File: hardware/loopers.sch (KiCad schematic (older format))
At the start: 2 parts

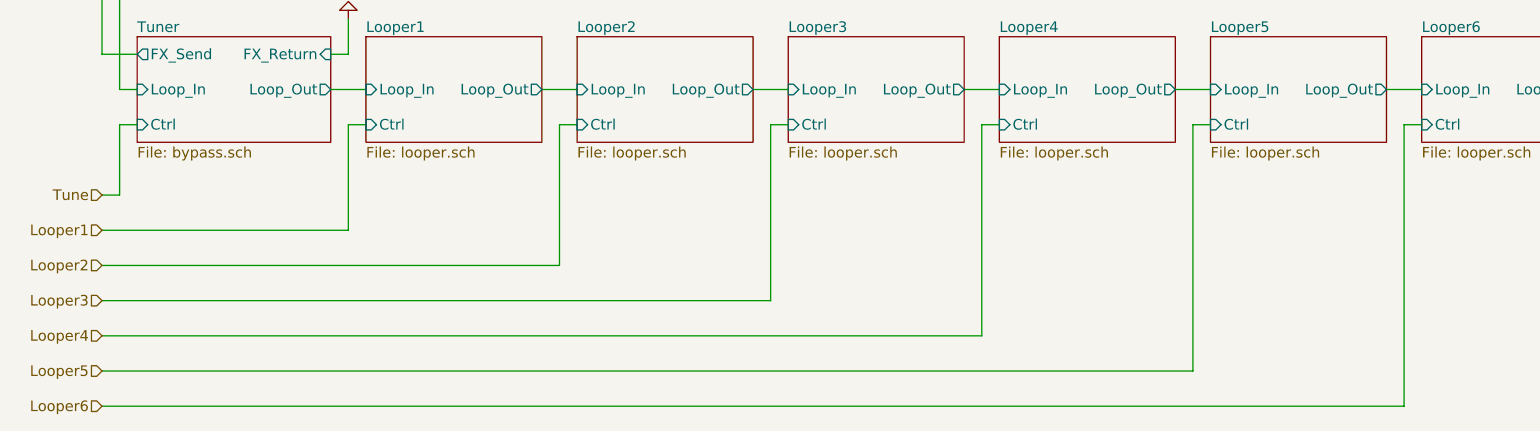
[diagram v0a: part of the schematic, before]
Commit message: Tidy up loopers schematic
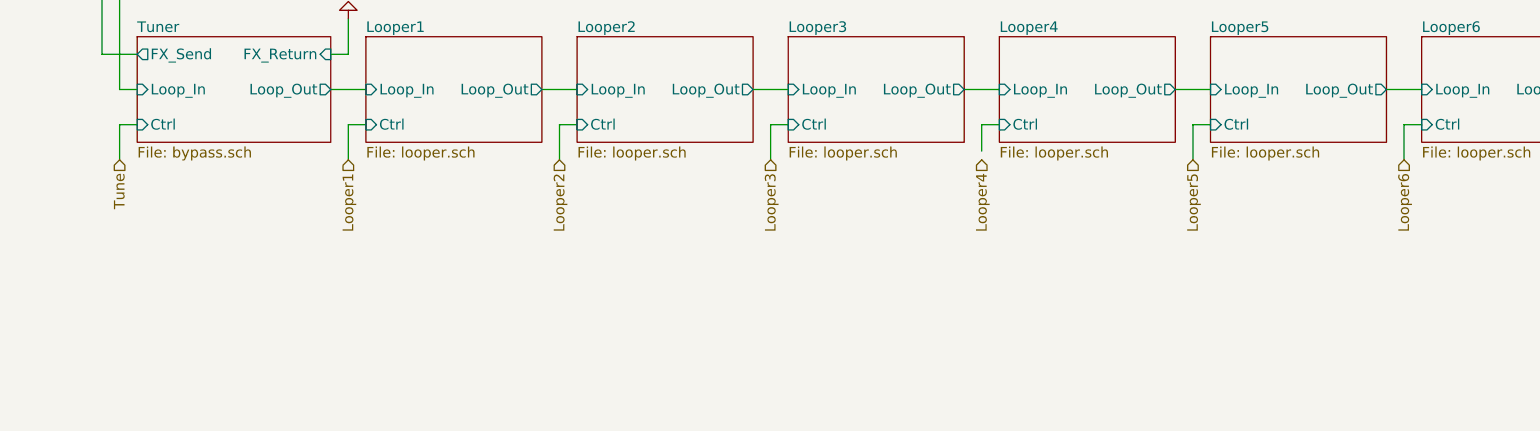
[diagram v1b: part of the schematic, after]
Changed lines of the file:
@@
 Wire Wire Line
 	2500 3200 2500 3000
-Text HLabel 1100 4000 0    60   Input ~ 0
+Text HLabel 1200 3800 3    60   Input ~ 0
 Tune
-Text HLabel 1100 4200 0    60   Input ~ 0
+Text HLabel 2500 3800 3    60   Input ~ 0
 Looper1
-Text HLabel 1100 4400 0    60   Input ~ 0
+Text HLabel 3700 3800 3    60   Input ~ 0
 Looper2
-Text HLabel 1100 4600 0    60   Input ~ 0
+Text HLabel 4900 3800 3    60   Input ~ 0
 Looper3
-Text HLabel 1100 4800 0    60   Input ~ 0
+Text HLabel 6100 3800 3    60   Input ~ 0
 Looper4
-Text HLabel 1100 5000 0    60   Input ~ 0
+Text HLabel 7300 3800 3    60   Input ~ 0
 Looper5
-Text HLabel 1100 5200 0    60   Input ~ 0
+Text HLabel 8500 3800 3    60   Input ~ 0
 Looper6
-Wire Wire Line
-	1200 4000 1200 3600
 Wire Wire Line
 	1200 3600 1300 3600
 Wire Wire Line
-	1100 4000 1200 4000
-Wire Wire Line
-	1100 4200 2500 4200
-Wire Wire Line
-	2500 4200 2500 3600
-Wire Wire Line
 	2500 3600 2600 3600
-Wire Wire Line
-	1100 4400 3700 4400
-Wire Wire Line
-	3700 4400 3700 3600
 Wire Wire Line
 	3700 3600 3800 3600
 Wire Wire Line
-	1100 4600 4900 4600
-Wire Wire Line
-	4900 4600 4900 3600
-Wire Wire Line
 	4900 3600 5000 3600
-Wire Wire Line
-	1100 4800 6100 4800
-Wire Wire Line
-	6100 4800 6100 3600
 Wire Wire Line
 	6100 3600 6200 3600
 Wire Wire Line
-	1100 5000 7300 5000
-Wire Wire Line
-	7300 5000 7300 3600
-Wire Wire Line
 	7300 3600 7400 3600
 Wire Wire Line
-	1100 5200 8500 5200
+	8500 3600 8600 3600
 Wire Wire Line
-	8500 5200 8500 3600
+	8500 3800 8500 3600
 Wire Wire Line
-	8500 3600 8600 3600
+	1200 3800 1200 3600
+Wire Wire Line
+	2500 3600 2500 3800
+Wire Wire Line
+	3700 3800 3700 3600
+Wire Wire Line
+	4900 3800 4900 3600
+Wire Wire Line
+	6100 3750 6100 3600
+Wire Wire Line
+	7300 3800 7300 3600
 $EndSCHEMATC

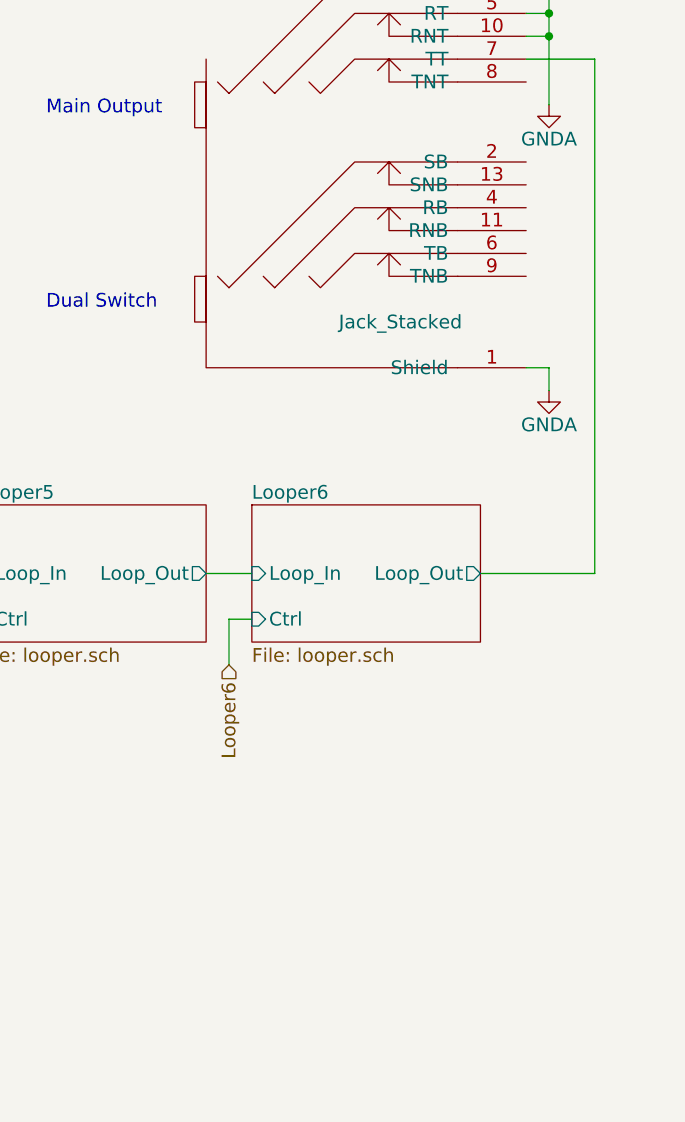
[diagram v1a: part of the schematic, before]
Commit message: Stub and integrate aux switch
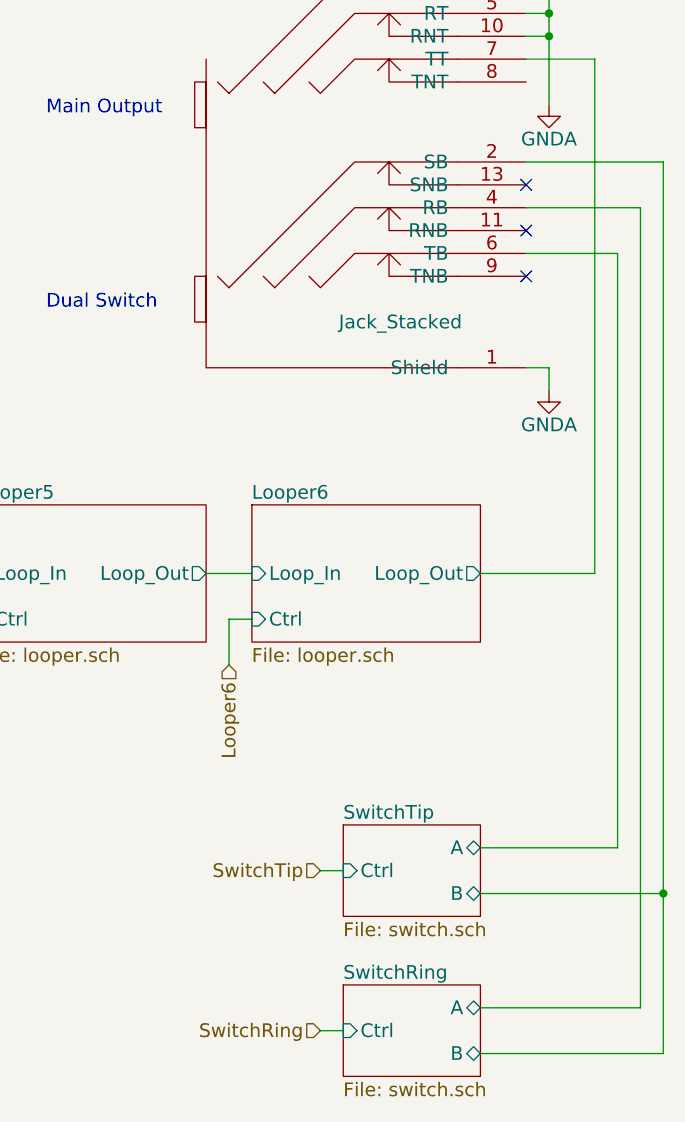
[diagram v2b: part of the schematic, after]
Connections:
- net SwitchRing/B: now reaches CON?.2 (SB)
- net SwitchRing/A: now reaches CON?.4 (RB)
- net SwitchTip/A: now reaches CON?.6 (TB)
- no-connect marks 0 -> 3
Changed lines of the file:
@@
 $Descr A4 11693 8268
 encoding utf-8
-Sheet 3 19
+Sheet 3 21
 Title ""
 Date ""
@@
 Wire Wire Line
 	7300 3800 7300 3600
+$Sheet
+S 9000 4500 600  400
+U 54E8DAE1
+F0 "SwitchTip" 60
+F1 "switch.sch" 60
+F2 "Ctrl" I L 9000 4700 60
+F3 "A" B R 9600 4600 60
+F4 "B" B R 9600 4800 60
+$EndSheet
+$Sheet
+S 9000 5200 600  400
+U 54E90580
+F0 "SwitchRing" 60
+F1 "switch.sch" 60
+F2 "Ctrl" I L 9000 5400 60
+F3 "A" B R 9600 5300 60
+F4 "B" B R 9600 5500 60
+$EndSheet
+Text HLabel 8900 4700 0    60   Input ~ 0
+SwitchTip
+Text HLabel 8900 5400 0    60   Input ~ 0
+SwitchRing
+Wire Wire Line
+	8900 4700 9000 4700
+Wire Wire Line
+	8900 5400 9000 5400
+Wire Wire Line
+	9800 1800 10300 1800
+Wire Wire Line
+	9800 2000 10200 2000
+Wire Wire Line
+	9800 1600 10400 1600
+NoConn ~ 9800 1700
+NoConn ~ 9800 1900
+NoConn ~ 9800 2100
+Wire Wire Line
+	9600 4600 10200 4600
+Wire Wire Line
+	10200 4600 10200 2000
+Wire Wire Line
+	10300 1800 10300 5300
+Wire Wire Line
+	10300 5300 9600 5300
+Wire Wire Line
+	9600 4800 10400 4800
+Wire Wire Line
+	10400 1600 10400 5500
+Wire Wire Line
+	10400 5500 9600 5500
+Connection ~ 10400 4800
 $EndSCHEMATC
